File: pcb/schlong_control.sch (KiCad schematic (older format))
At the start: 36 parts, among them P1 Power Connector (120V AC), P2 Input, P3 Output, U1 74HC595, U2 MOC3063M, U3 MOC3063M, U4 MOC3063M, U5 MOC3063M, U6 MOC3063M, U7 LM7805

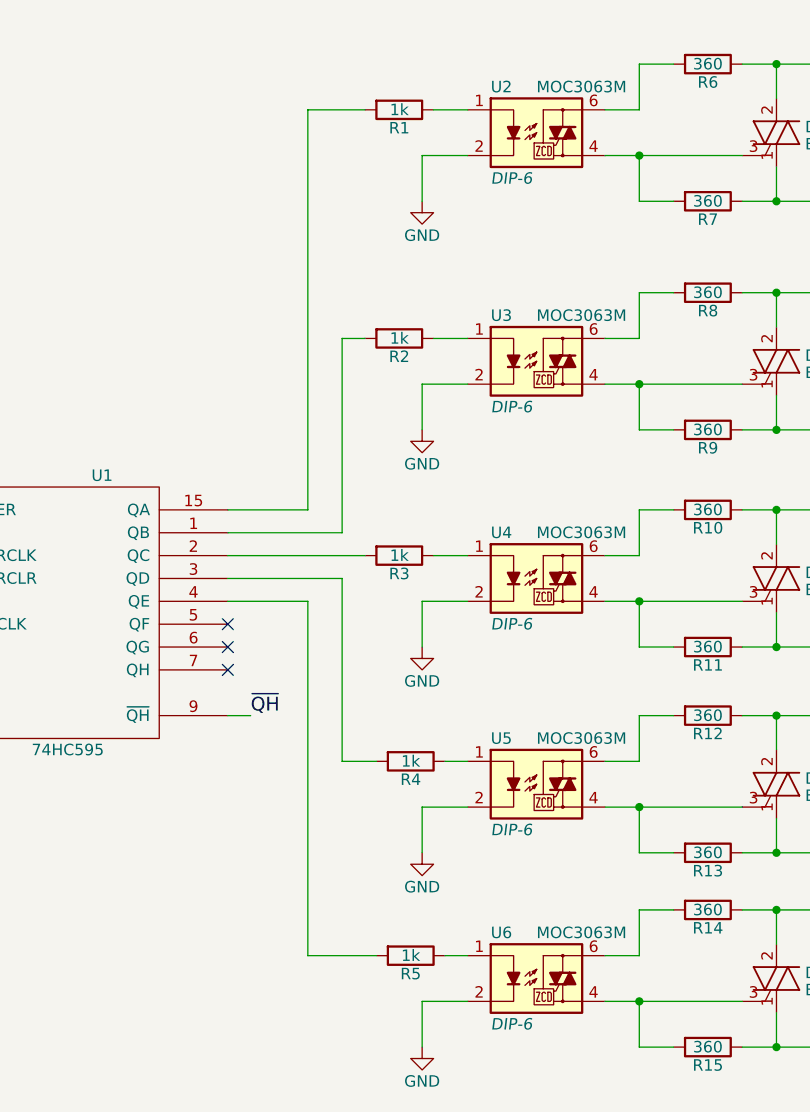
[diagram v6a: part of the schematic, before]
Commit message: reduce moc3063 led resistor from 1k to 510R
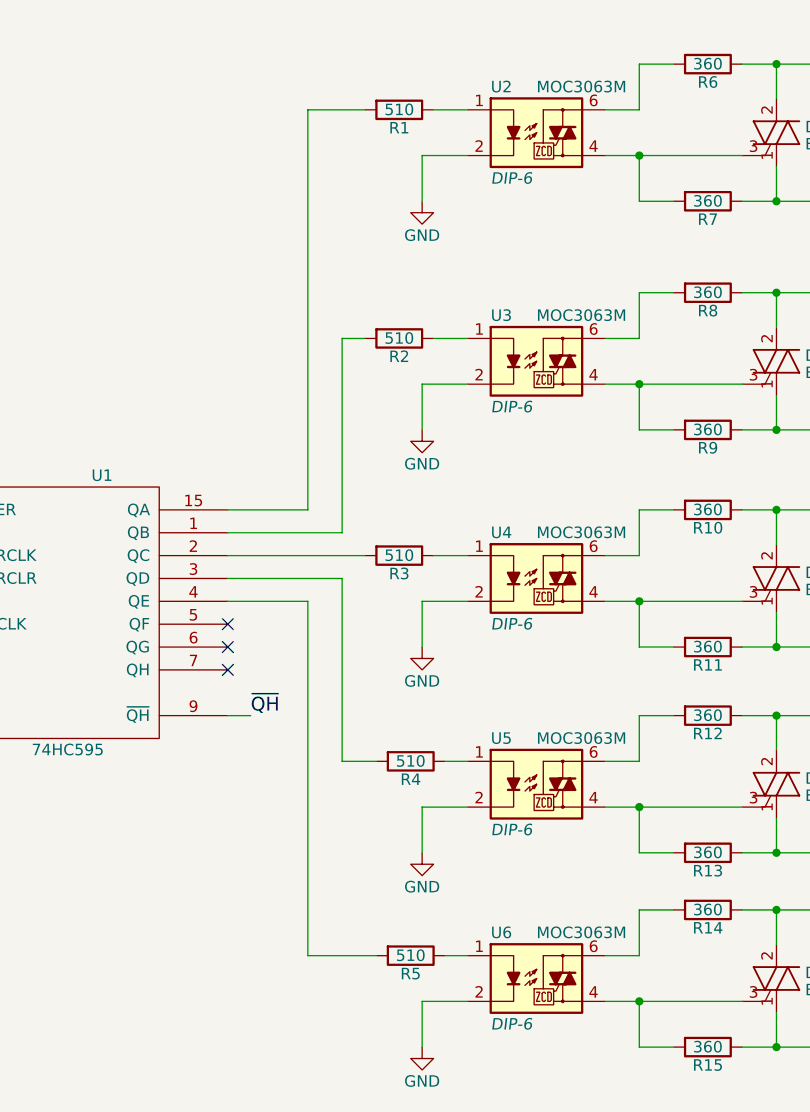
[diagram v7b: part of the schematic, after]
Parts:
- R1, R2, R3, R4, R5: value 1k -> 510
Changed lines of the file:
@@
 P 4750 1150
 F 0 "R1" V 4830 1150 50  0000 C CNN
-F 1 "1k" V 4750 1150 50  0000 C CNN
+F 1 "510" V 4750 1150 50  0000 C CNN
 F 2 "" V 4680 1150 50  0000 C CNN
 F 3 "" H 4750 1150 50  0000 C CNN
@@
 P 4750 2150
 F 0 "R2" V 4830 2150 50  0000 C CNN
-F 1 "1k" V 4750 2150 50  0000 C CNN
+F 1 "510" V 4750 2150 50  0000 C CNN
 F 2 "" V 4680 2150 50  0000 C CNN
 F 3 "" H 4750 2150 50  0000 C CNN
@@
 P 4750 3100
 F 0 "R3" V 4830 3100 50  0000 C CNN
-F 1 "1k" V 4750 3100 50  0000 C CNN
+F 1 "510" V 4750 3100 50  0000 C CNN
 F 2 "" V 4680 3100 50  0000 C CNN
 F 3 "" H 4750 3100 50  0000 C CNN
@@
 P 4800 4000
 F 0 "R4" V 4880 4000 50  0000 C CNN
-F 1 "1k" V 4800 4000 50  0000 C CNN
+F 1 "510" V 4800 4000 50  0000 C CNN
 F 2 "" V 4730 4000 50  0000 C CNN
 F 3 "" H 4800 4000 50  0000 C CNN
@@
 P 4800 4850
 F 0 "R5" V 4880 4850 50  0000 C CNN
-F 1 "1k" V 4800 4850 50  0000 C CNN
+F 1 "510" V 4800 4850 50  0000 C CNN
 F 2 "" V 4730 4850 50  0000 C CNN
 F 3 "" H 4800 4850 50  0000 C CNN
